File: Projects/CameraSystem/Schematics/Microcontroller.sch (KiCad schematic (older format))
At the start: 29 parts, among them J2 Conn_02x03_Odd_Even, J3 Conn_01x02, J4 Conn_01x03, J5 Conn_01x02, U3 ATMEGA16A-AU, Y2 ABLS2-10.000MHZ-D4Y-T

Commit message: feat: symbol assignment updated
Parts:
- C10, C11, C12, C13, C14, C15, C16, C17: footprint Capacitor_SMD:C_0603_1608Metric_Pad1.05x0.95mm_HandSolder -> digikey-footprints:0603
- D5: footprint SOT23-3 -> custom-footprints:SOT−23_(TO−236)
- D6: footprint (none) -> custom-footprints:LED_APG1608
- R10, R11, R12, R16, R19, R20, R21, R6, R7, R8, R9: footprint Resistor_SMD:R_0603_1608Metric_Pad1.05x0.95mm_HandSolder -> digikey-footprints:0603
- U3: footprint TQFP44 -> (none)
- Y2: footprint F -> (none)
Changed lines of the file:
@@
 F 0 "U3" H 4300 5280 50  0000 L BNN
 F 1 "ATMEGA16A-AU" H 5800 1450 50  0000 L BNN
-F 2 "TQFP44" H 5250 3400 50  0001 C CIN
+F 2 "" H 5250 3400 50  0001 C CIN
 F 3 "" H 5250 3400 50  0001 C CNN
 	1    5250 3400
@@
 F 0 "R8" V 2080 1200 50  0000 C CNN
 F 1 "10k" V 2000 1200 50  0000 C CNN
-F 2 "Resistor_SMD:R_0603_1608Metric_Pad1.05x0.95mm_HandSolder" V 1930 1200 50  0001 C CNN
+F 2 "digikey-footprints:0603" V 1930 1200 50  0001 C CNN
 F 3 "" H 2000 1200 50  0001 C CNN
 	1    2000 1200
@@
 F 0 "D5" H 3000 1300 50  0000 C CNN
 F 1 "BZX84C3V3LT1G" H 3000 1100 50  0000 C CNN
-F 2 "SOT23-3" H 3000 1400 50  0000 C CNN
+F 2 "custom-footprints:SOT−23_(TO−236)" H 3000 1400 50  0001 C CNN
 F 3 "" H 3000 1200 50  0001 C CNN
 	1    3000 1200
@@
 F 0 "C12" H 3625 3350 50  0000 L CNN
 F 1 "27p" H 3625 3150 50  0000 L CNN
-F 2 "Capacitor_SMD:C_0603_1608Metric_Pad1.05x0.95mm_HandSolder" H 3638 3100 50  0001 C CNN
+F 2 "digikey-footprints:0603" H 3638 3100 50  0001 C CNN
 F 3 "" H 3600 3250 50  0001 C CNN
 	1    3600 3250
@@
 F 0 "C11" H 2975 3350 50  0000 L CNN
 F 1 "27p" H 2975 3150 50  0000 L CNN
-F 2 "Capacitor_SMD:C_0603_1608Metric_Pad1.05x0.95mm_HandSolder" H 2988 3100 50  0001 C CNN
+F 2 "digikey-footprints:0603" H 2988 3100 50  0001 C CNN
 F 3 "" H 2950 3250 50  0001 C CNN
 	1    2950 3250
@@
 F 0 "Y2" H 3300 3150 50  0000 C CNN
 F 1 "ABLS2-10.000MHZ-D4Y-T" H 3500 3250 50  0000 C CNN
-F 2 "F" H 3300 3000 50  0001 C CNN
+F 2 "" H 3300 3000 50  0001 C CNN
 F 3 "" H 3300 3000 50  0001 C CNN
 	1    3300 3000
@@
 F 0 "C14" H 4075 1150 50  0000 L CNN
 F 1 "100n" H 4075 950 50  0000 L CNN
-F 2 "Capacitor_SMD:C_0603_1608Metric_Pad1.05x0.95mm_HandSolder" H 4088 900 50  0001 C CNN
+F 2 "digikey-footprints:0603" H 4088 900 50  0001 C CNN
 F 3 "" H 4050 1050 50  0001 C CNN
 	1    4050 1050
@@
 F 0 "R9" V 2080 2050 50  0000 C CNN
 F 1 "330" V 2000 2050 50  0000 C CNN
-F 2 "Resistor_SMD:R_0603_1608Metric_Pad1.05x0.95mm_HandSolder" V 1930 2050 50  0001 C CNN
+F 2 "digikey-footprints:0603" V 1930 2050 50  0001 C CNN
 F 3 "" H 2000 2050 50  0001 C CNN
 	1    2000 2050
@@
 F 0 "R10" V 2680 4950 50  0000 C CNN
 F 1 "330" V 2600 4950 50  0000 C CNN
-F 2 "Resistor_SMD:R_0603_1608Metric_Pad1.05x0.95mm_HandSolder" V 2530 4950 50  0001 C CNN
+F 2 "digikey-footprints:0603" V 2530 4950 50  0001 C CNN
 F 3 "" H 2600 4950 50  0001 C CNN
 	1    2600 4950
@@
 F 0 "R6" V 1480 4750 50  0000 C CNN
 F 1 "330" V 1400 4750 50  0000 C CNN
-F 2 "Resistor_SMD:R_0603_1608Metric_Pad1.05x0.95mm_HandSolder" V 1330 4750 50  0001 C CNN
+F 2 "digikey-footprints:0603" V 1330 4750 50  0001 C CNN
 F 3 "" H 1400 4750 50  0001 C CNN
 	1    1400 4750
@@
 F 0 "R7" V 1480 4950 50  0000 C CNN
 F 1 "330" V 1400 4950 50  0000 C CNN
-F 2 "Resistor_SMD:R_0603_1608Metric_Pad1.05x0.95mm_HandSolder" V 1330 4950 50  0001 C CNN
+F 2 "digikey-footprints:0603" V 1330 4950 50  0001 C CNN
 F 3 "" H 1400 4950 50  0001 C CNN
 	1    1400 4950
@@
 F 0 "C15" H 4375 1150 50  0000 L CNN
 F 1 "100n" H 4375 950 50  0000 L CNN
-F 2 "Capacitor_SMD:C_0603_1608Metric_Pad1.05x0.95mm_HandSolder" H 4388 900 50  0001 C CNN
+F 2 "digikey-footprints:0603" H 4388 900 50  0001 C CNN
 F 3 "" H 4350 1050 50  0001 C CNN
 	1    4350 1050
@@
 F 0 "C16" H 4675 1150 50  0000 L CNN
 F 1 "100n" H 4675 950 50  0000 L CNN
-F 2 "Capacitor_SMD:C_0603_1608Metric_Pad1.05x0.95mm_HandSolder" H 4688 900 50  0001 C CNN
+F 2 "digikey-footprints:0603" H 4688 900 50  0001 C CNN
 F 3 "" H 4650 1050 50  0001 C CNN
 	1    4650 1050
@@
 F 0 "C17" H 5625 1200 50  0000 L CNN
 F 1 "100n" H 5625 1000 50  0000 L CNN
-F 2 "Capacitor_SMD:C_0603_1608Metric_Pad1.05x0.95mm_HandSolder" H 5638 950 50  0001 C CNN
+F 2 "digikey-footprints:0603" H 5638 950 50  0001 C CNN
 F 3 "" H 5600 1100 50  0001 C CNN
 	1    5600 1100
@@
 F 0 "R11" V 3380 2500 50  0000 C CNN
 F 1 "1M" V 3300 2500 50  0000 C CNN
-F 2 "Resistor_SMD:R_0603_1608Metric_Pad1.05x0.95mm_HandSolder" V 3230 2500 50  0001 C CNN
+F 2 "digikey-footprints:0603" V 3230 2500 50  0001 C CNN
 F 3 "" H 3300 2500 50  0001 C CNN
 	1    3300 2500
@@
 F 0 "D6" H 8400 4100 50  0000 C CNN
 F 1 "APG1608SYKC/T" H 8400 3900 50  0000 C CNN
-F 2 "" H 8400 4000 50  0001 C CNN
+F 2 "custom-footprints:LED_APG1608" H 8400 4000 50  0001 C CNN
 F 3 "" H 8400 4000 50  0001 C CNN
 	1    8400 4000
@@
 F 0 "R21" V 8480 3650 50  0000 C CNN
 F 1 "560" V 8400 3650 50  0000 C CNN
-F 2 "Resistor_SMD:R_0603_1608Metric_Pad1.05x0.95mm_HandSolder" V 8330 3650 50  0001 C CNN
+F 2 "digikey-footprints:0603" V 8330 3650 50  0001 C CNN
 F 3 "" H 8400 3650 50  0001 C CNN
 	1    8400 3650
@@
 F 0 "R19" V 7530 2950 50  0000 C CNN
 F 1 "2K2" V 7450 2950 50  0000 C CNN
-F 2 "Resistor_SMD:R_0603_1608Metric_Pad1.05x0.95mm_HandSolder" V 7380 2950 50  0001 C CNN
+F 2 "digikey-footprints:0603" V 7380 2950 50  0001 C CNN
 F 3 "" H 7450 2950 50  0001 C CNN
 	1    7450 2950
@@
 F 0 "R20" V 7730 2950 50  0000 C CNN
 F 1 "2K2" V 7650 2950 50  0000 C CNN
-F 2 "Resistor_SMD:R_0603_1608Metric_Pad1.05x0.95mm_HandSolder" V 7580 2950 50  0001 C CNN
+F 2 "digikey-footprints:0603" V 7580 2950 50  0001 C CNN
 F 3 "" H 7650 2950 50  0001 C CNN
 	1    7650 2950
@@
 F 0 "C10" H 2425 2800 50  0000 L CNN
 F 1 "100n" H 2425 2600 50  0000 L CNN
-F 2 "Capacitor_SMD:C_0603_1608Metric_Pad1.05x0.95mm_HandSolder" H 2438 2550 50  0001 C CNN
+F 2 "digikey-footprints:0603" H 2438 2550 50  0001 C CNN
 F 3 "" H 2400 2700 50  0001 C CNN
 	1    2400 2700
@@
 F 0 "R12" V 6680 2900 50  0000 C CNN
 F 1 "10k" V 6600 2900 50  0000 C CNN
-F 2 "Resistor_SMD:R_0603_1608Metric_Pad1.05x0.95mm_HandSolder" V 6530 2900 50  0001 C CNN
+F 2 "digikey-footprints:0603" V 6530 2900 50  0001 C CNN
 F 3 "" H 6600 2900 50  0001 C CNN
 	1    6600 2900
@@
 F 0 "R16" V 6930 2800 50  0000 C CNN
 F 1 "10k" V 6850 2800 50  0000 C CNN
-F 2 "Resistor_SMD:R_0603_1608Metric_Pad1.05x0.95mm_HandSolder" V 6780 2800 50  0001 C CNN
+F 2 "digikey-footprints:0603" V 6780 2800 50  0001 C CNN
 F 3 "" H 6850 2800 50  0001 C CNN
 	1    6850 2800
@@
 F 0 "C13" H 3975 3250 50  0000 L CNN
 F 1 "100n" H 3975 3050 50  0000 L CNN
-F 2 "Capacitor_SMD:C_0603_1608Metric_Pad1.05x0.95mm_HandSolder" H 3988 3000 50  0001 C CNN
+F 2 "digikey-footprints:0603" H 3988 3000 50  0001 C CNN
 F 3 "" H 3950 3150 50  0001 C CNN
 	1    3950 3150

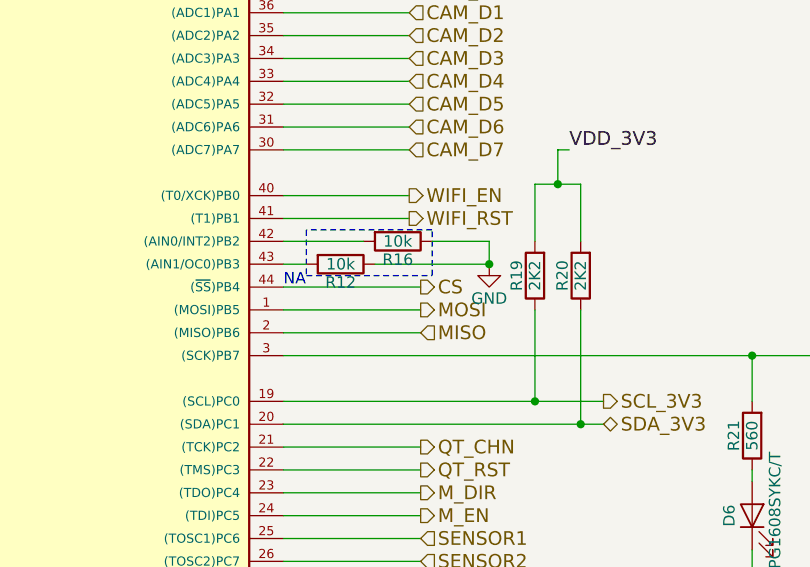
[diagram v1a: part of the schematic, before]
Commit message: feat: assign footprints
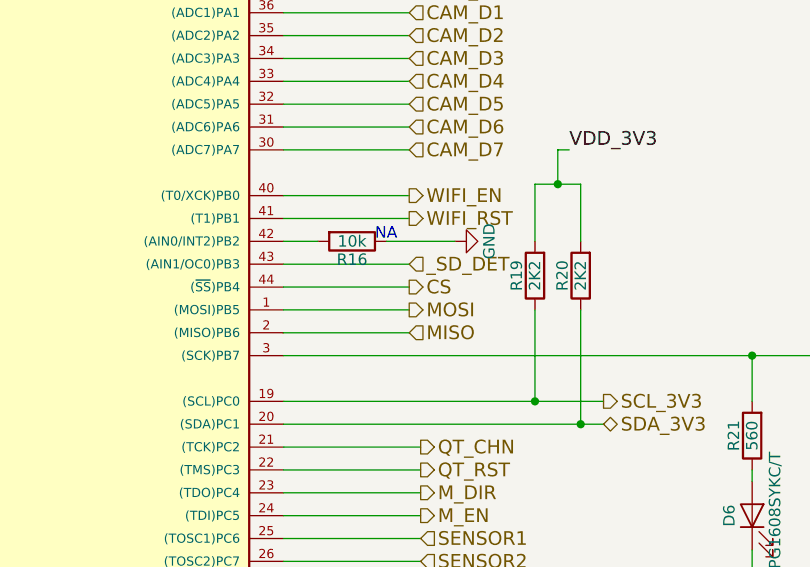
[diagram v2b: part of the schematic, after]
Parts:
- removed R12: 10k, digikey-footprints:0603, symbol Device:R
- J2: footprint (none) -> Pin_Headers:Pin_Header_Straight_2x03_Pitch2.54mm
- J3, J5: footprint (none) -> Pin_Headers:Pin_Header_Straight_1x02_Pitch2.54mm
- J4: footprint (none) -> Pin_Headers:Pin_Header_Straight_1x03_Pitch2.54mm
- U3: footprint (none) -> custom-footprints:QFP80P1200X1200X120-44N
- Y2: footprint (none) -> custom-footprints:ABLS2-10.000MHZ-D4Y-T
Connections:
- net labels added: _SD_DET
- wire segments 140 -> 138
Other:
- moved on the sheet: R16
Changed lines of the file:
@@
 F 0 "U3" H 4300 5280 50  0000 L BNN
 F 1 "ATMEGA16A-AU" H 5800 1450 50  0000 L BNN
-F 2 "" H 5250 3400 50  0001 C CIN
+F 2 "custom-footprints:QFP80P1200X1200X120-44N" H 5250 3400 50  0001 C CIN
 F 3 "" H 5250 3400 50  0001 C CNN
 	1    5250 3400
@@
 F 0 "Y2" H 3300 3150 50  0000 C CNN
 F 1 "ABLS2-10.000MHZ-D4Y-T" H 3500 3250 50  0000 C CNN
-F 2 "" H 3300 3000 50  0001 C CNN
+F 2 "custom-footprints:ABLS2-10.000MHZ-D4Y-T" H 3300 3000 50  0001 C CNN
 F 3 "" H 3300 3000 50  0001 C CNN
 	1    3300 3000
@@
 Text Label 6700 800  0    60   ~ 0
 VDD_3V3
-Text HLabel 6950 3100 2    60   Output ~ 0
+Text HLabel 6900 3100 2    60   Output ~ 0
 MOSI
-Text HLabel 6950 3200 2    60   Input ~ 0
+Text HLabel 6900 3200 2    60   Input ~ 0
 MISO
 Text HLabel 8750 3300 2    60   Output ~ 0
@@
 	1    0    0    -1
 $EndComp
-Text HLabel 6950 3000 2    60   Output ~ 0
+Text HLabel 6900 3000 2    60   Output ~ 0
 CS
 Wire Wire Line
@@
 	6250 800  6700 800
 Wire Wire Line
-	6350 3100 6950 3100
-Wire Wire Line
-	6350 3200 6950 3200
+	6350 3100 6900 3100
+Wire Wire Line
+	6350 3200 6900 3200
 Wire Wire Line
 	6350 3300 8400 3300
@@
 	8400 4150 8400 4300
 Wire Wire Line
-	6350 3000 6950 3000
+	6350 3000 6900 3000
 Wire Wire Line
 	8400 3300 8400 3500
@@
 F 0 "J3" H 10130 3792 50  0000 L CNN
 F 1 "Conn_01x02" H 10130 3701 50  0000 L CNN
-F 2 "" H 10050 3800 50  0001 C CNN
+F 2 "Pin_Headers:Pin_Header_Straight_1x02_Pitch2.54mm" H 10050 3800 50  0001 C CNN
 F 3 "~" H 10050 3800 50  0001 C CNN
 	1    10050 3800
@@
 F 0 "J4" H 10130 4342 50  0000 L CNN
 F 1 "Conn_01x03" H 10130 4251 50  0000 L CNN
-F 2 "" H 10050 4300 50  0001 C CNN
+F 2 "Pin_Headers:Pin_Header_Straight_1x03_Pitch2.54mm" H 10050 4300 50  0001 C CNN
 F 3 "~" H 10050 4300 50  0001 C CNN
 	1    10050 4300
@@
 F 0 "J5" H 10130 4692 50  0000 L CNN
 F 1 "Conn_01x02" H 10130 4601 50  0000 L CNN
-F 2 "" H 10050 4700 50  0001 C CNN
+F 2 "Pin_Headers:Pin_Header_Straight_1x02_Pitch2.54mm" H 10050 4700 50  0001 C CNN
 F 3 "~" H 10050 4700 50  0001 C CNN
 	1    10050 4700
@@
 F 0 "J2" H 1950 4700 50  0000 C CNN
 F 1 "Conn_02x03_Odd_Even" H 1950 5250 50  0000 C CNN
-F 2 "" H 1900 4950 50  0001 C CNN
+F 2 "Pin_Headers:Pin_Header_Straight_2x03_Pitch2.54mm" H 1900 4950 50  0001 C CNN
 F 3 "~" H 1900 4950 50  0001 C CNN
 	1    1900 4950
@@
 $EndComp
 $Comp
-L Device:R R12
-U 1 1 5BC2AC35
-P 6600 2900
-F 0 "R12" V 6680 2900 50  0000 C CNN
-F 1 "10k" V 6600 2900 50  0000 C CNN
-F 2 "digikey-footprints:0603" V 6530 2900 50  0001 C CNN
-F 3 "" H 6600 2900 50  0001 C CNN
-	1    6600 2900
-	0    1    1    0
-$EndComp
-$Comp
 L Device:R R16
 U 1 1 5BC2ACBF
-P 6850 2800
-F 0 "R16" V 6930 2800 50  0000 C CNN
-F 1 "10k" V 6850 2800 50  0000 C CNN
-F 2 "digikey-footprints:0603" V 6780 2800 50  0001 C CNN
-F 3 "" H 6850 2800 50  0001 C CNN
-	1    6850 2800
+P 6650 2800
+F 0 "R16" V 6730 2800 50  0000 C CNN
+F 1 "10k" V 6650 2800 50  0000 C CNN
+F 2 "digikey-footprints:0603" V 6580 2800 50  0001 C CNN
+F 3 "" H 6650 2800 50  0001 C CNN
+	1    6650 2800
 	0    1    1    0
 $EndComp
-Text Notes 6350 3000 0    50   ~ 0
+Text Notes 6750 2800 0    50   ~ 0
 NA
-Wire Wire Line
-	6350 2900 6450 2900
-Wire Wire Line
-	6700 2800 6350 2800
-Wire Wire Line
-	7250 2900 7250 2800
-Wire Wire Line
-	7250 2800 7000 2800
-Wire Wire Line
-	6750 2900 7250 2900
 $Comp
 L power:GND #PWR06
 U 1 1 5BC56CC7
-P 7250 2900
-F 0 "#PWR06" H 7250 2650 50  0001 C CNN
-F 1 "GND" H 7250 2750 50  0000 C CNN
-F 2 "" H 7250 2900 50  0001 C CNN
-F 3 "" H 7250 2900 50  0001 C CNN
-	1    7250 2900
-	1    0    0    -1
-$EndComp
-Connection ~ 7250 2900
-Wire Notes Line
-	6450 2750 6450 2950
-Wire Notes Line
-	6450 2950 7000 2950
-Wire Notes Line
-	7000 2950 7000 2750
-Wire Notes Line
-	7000 2750 6450 2750
+P 7100 2800
+F 0 "#PWR06" H 7100 2550 50  0001 C CNN
+F 1 "GND" H 7100 2650 50  0000 C CNN
+F 2 "" H 7100 2800 50  0001 C CNN
+F 3 "" H 7100 2800 50  0001 C CNN
+	1    7100 2800
+	0    -1   -1   0
+$EndComp
 $Comp
 L Device:C C13
@@
 Wire Wire Line
 	6350 4100 6950 4100
+Wire Wire Line
+	6800 2800 7100 2800
+Text HLabel 6900 2900 2    60   Input ~ 0
+_SD_DET
+Wire Wire Line
+	6350 2900 6900 2900
+Wire Wire Line
+	6500 2800 6350 2800
 $EndSCHEMATC

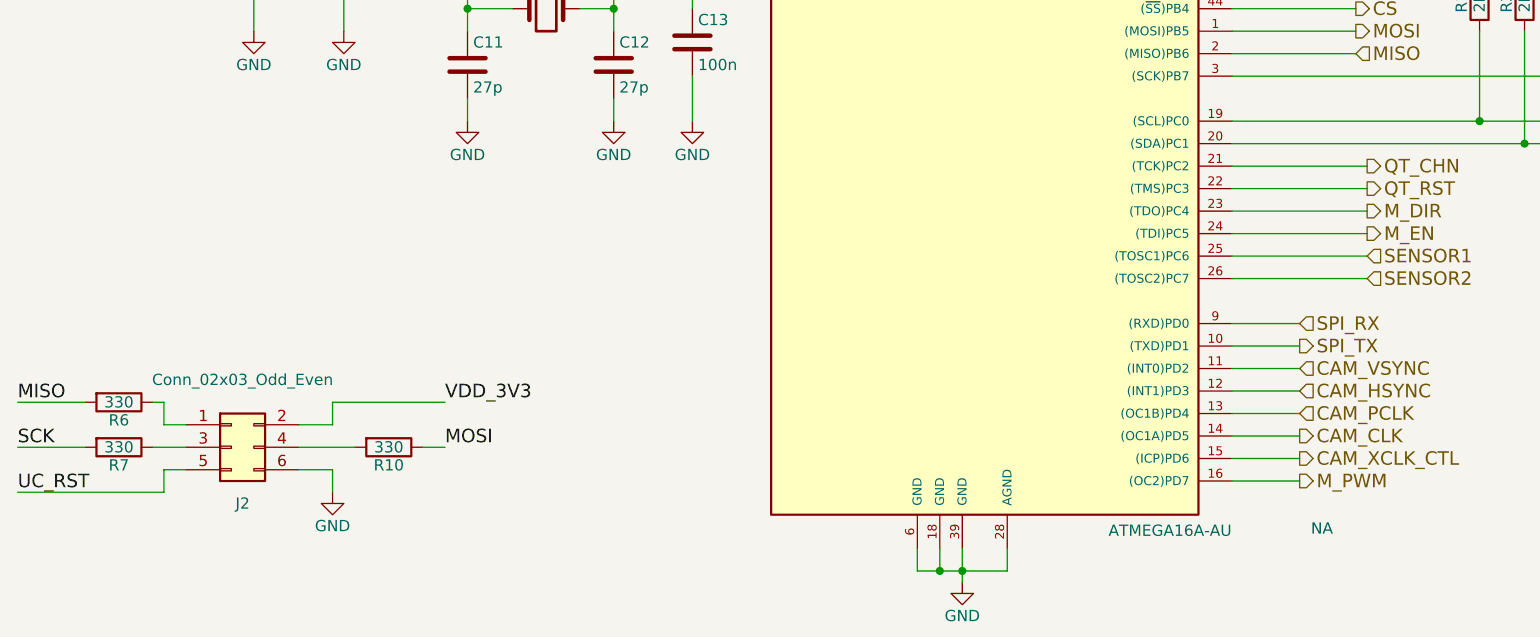
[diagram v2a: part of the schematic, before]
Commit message: Camera System QT Pad schematic reviewed
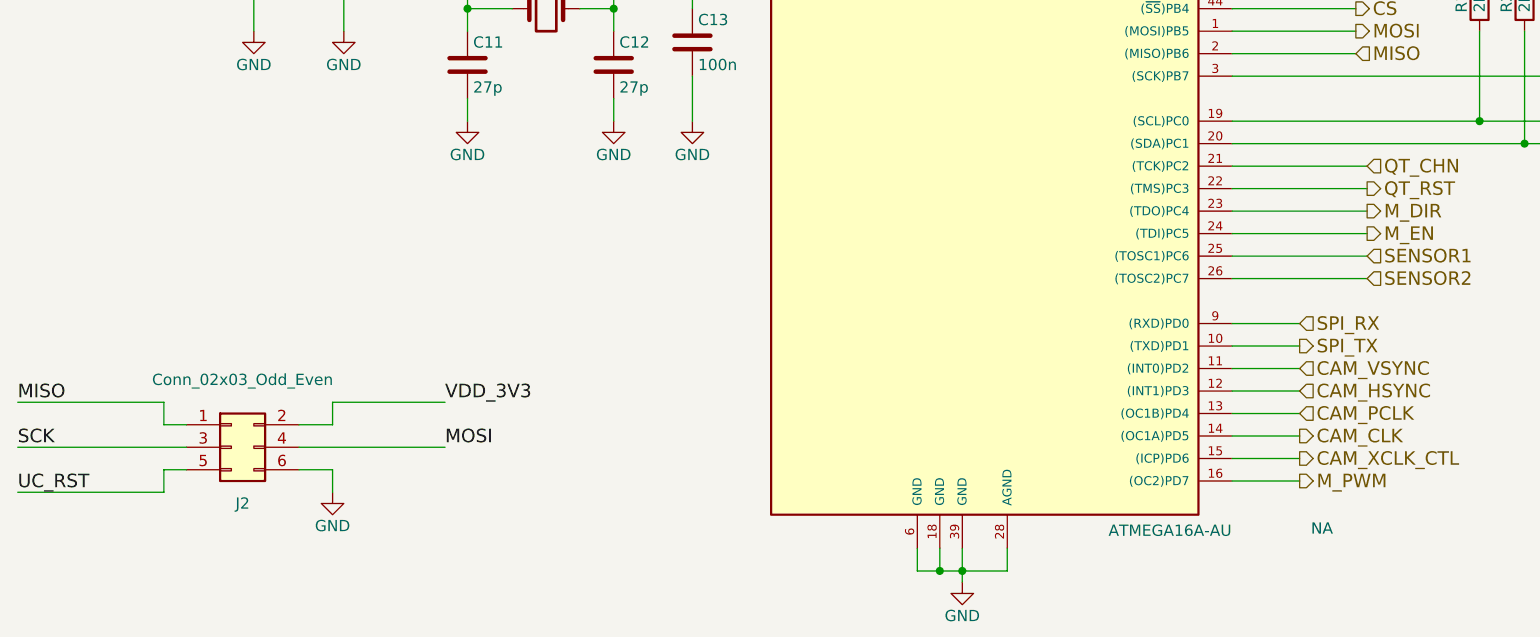
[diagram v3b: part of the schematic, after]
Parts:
- removed R10, R6, R7: 330, digikey-footprints:0603, symbol Device:R
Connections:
- wire segments 138 -> 135
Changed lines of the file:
@@
 UC_RST
-$Comp
-L Device:R R10
-U 1 1 5BB8F677
-P 2600 4950
-F 0 "R10" V 2680 4950 50  0000 C CNN
-F 1 "330" V 2600 4950 50  0000 C CNN
-F 2 "digikey-footprints:0603" V 2530 4950 50  0001 C CNN
-F 3 "" H 2600 4950 50  0001 C CNN
-	1    2600 4950
-	0    1    1    0
-$EndComp
-$Comp
-L Device:R R6
-U 1 1 5BB8F70D
-P 1400 4750
-F 0 "R6" V 1480 4750 50  0000 C CNN
-F 1 "330" V 1400 4750 50  0000 C CNN
-F 2 "digikey-footprints:0603" V 1330 4750 50  0001 C CNN
-F 3 "" H 1400 4750 50  0001 C CNN
-	1    1400 4750
-	0    1    1    0
-$EndComp
-$Comp
-L Device:R R7
-U 1 1 5BB8F779
-P 1400 4950
-F 0 "R7" V 1480 4950 50  0000 C CNN
-F 1 "330" V 1400 4950 50  0000 C CNN
-F 2 "digikey-footprints:0603" V 1330 4950 50  0001 C CNN
-F 3 "" H 1400 4950 50  0001 C CNN
-	1    1400 4950
-	0    1    1    0
-$EndComp
 $Comp
 L Device:C C15
@@
 Connection ~ 2000 2900
 Wire Wire Line
-	1550 4950 1700 4950
-Wire Wire Line
 	1700 4850 1600 4850
 Wire Wire Line
 	1600 4850 1600 4750
 Wire Wire Line
-	1600 4750 1550 4750
-Wire Wire Line
-	1250 4750 950  4750
-Wire Wire Line
-	1250 4950 950  4950
-Wire Wire Line
 	1700 5050 1600 5050
 Wire Wire Line
@@
 	1600 5150 950  5150
 Wire Wire Line
-	2200 4950 2450 4950
-Wire Wire Line
 	2200 4850 2350 4850
 Wire Wire Line
@@
 Wire Wire Line
 	2350 4750 2850 4750
-Wire Wire Line
-	2750 4950 2850 4950
 Wire Wire Line
 	2200 5050 2350 5050
@@
 Wire Wire Line
 	6350 3800 6950 3800
-Text HLabel 6950 3700 2    60   Output ~ 0
+Text HLabel 6950 3700 2    60   Input ~ 0
 QT_CHN
 Text HLabel 6950 3800 2    60   Output ~ 0
@@
 Wire Wire Line
 	6500 2800 6350 2800
+Wire Wire Line
+	950  4750 1600 4750
+Wire Wire Line
+	950  4950 1700 4950
+Wire Wire Line
+	2200 4950 2850 4950
 $EndSCHEMATC
